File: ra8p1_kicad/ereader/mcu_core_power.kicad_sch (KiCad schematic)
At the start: 17 parts, among them U1 R7KA8P1KFLCAC#UC0

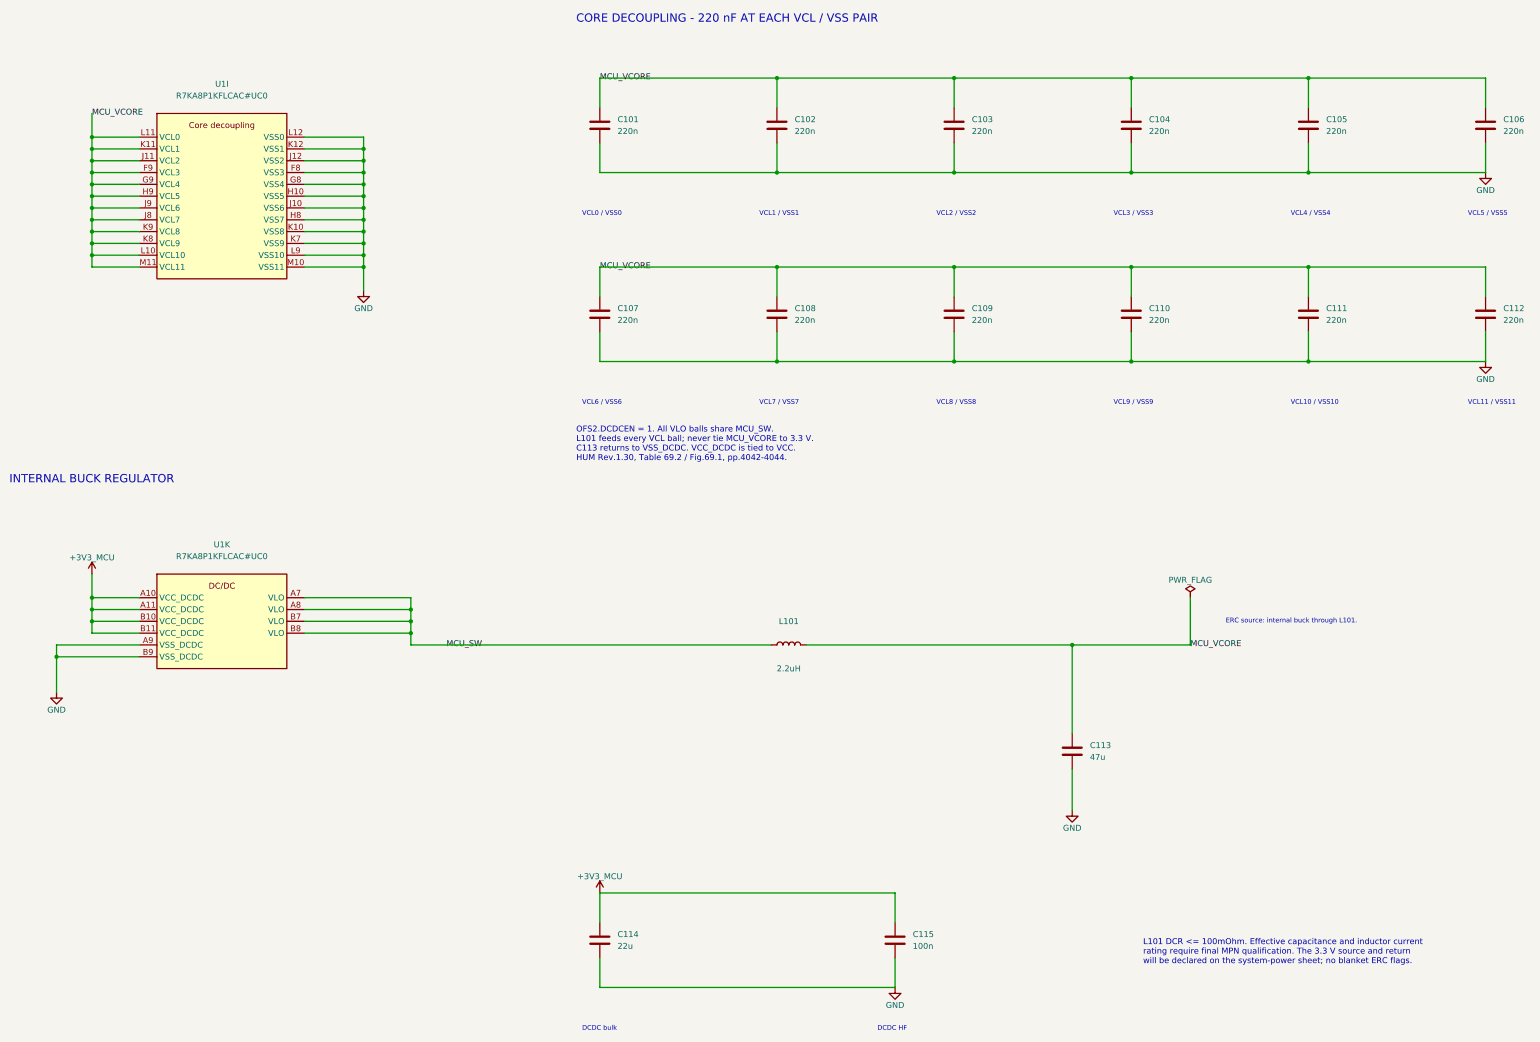
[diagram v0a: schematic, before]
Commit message: feat(hardware): add RA8P1 boot debug draft and refine schematic presentation
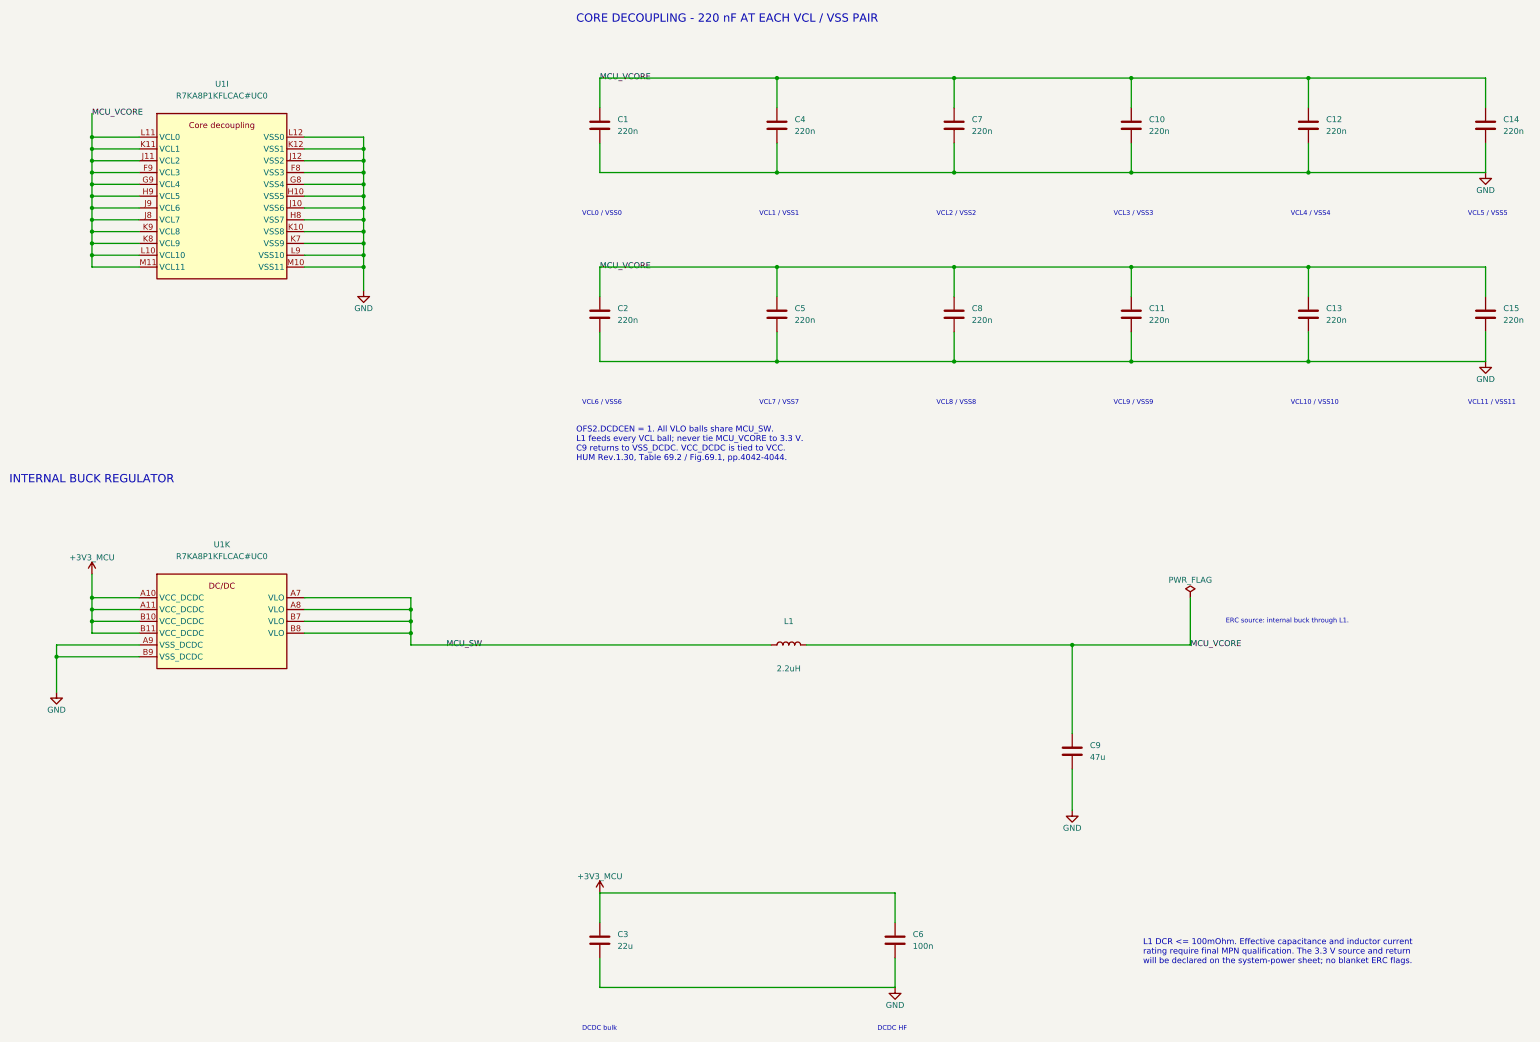
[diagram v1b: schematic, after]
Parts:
- L1: renamed from L101; Manufacturer_Name (none) -> TDK; Manufacturer_Part_Number (none) -> SPM5020T-2R2M-LR; Selection_Basis (none) -> Renesas R01AN7883EU0110 Table 3; 2.2uH +/-20%, DCR max 40.7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
- renumbered C101 to C1, C104 to C10, C110 to C11, C105 to C12, C111 to C13, C106 to C14, C112 to C15, C107 to C2, C114 to C3, C102 to C4, C108 to C5, C115 to C6, C103 to C7, C109 to C8, C113 to C9
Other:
- note added: "ERC source: internal buck through L1."
- note added: "L1 DCR <= 100mOhm. Effective capacitance and inductor current rating require final MPN qualification. The 3.3 V source and return will be declared on the system-power sheet; no blanket ERC flags."
- note added: "OFS2.DCDCEN = 1. All VLO balls share MCU_SW. L1 feeds every VCL ball; never tie MCU_VCORE to 3.3 V. C9 returns to VSS_DCDC. VCC_DCDC is tied to VCC. HUM Rev.1.30, Table 69.2 / Fig.69.1, pp.4042-4044."
- note removed: "ERC source: internal buck through L101."
- note removed: "L101 DCR <= 100mOhm. Effective capacitance and inductor current rating require final MPN qualification. The 3.3 V source and return will be declared on the system-power sheet; no blanket ERC flags."
- note removed: "OFS2.DCDCEN = 1. All VLO balls share MCU_SW. L101 feeds every VCL ball; never tie MCU_VCORE to 3.3 V. C113 returns to VSS_DCDC. VCC_DCDC is tied to VCC. HUM Rev.1.30, Table 69.2 / Fig.69.1, pp.4042-4044."

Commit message: feat(hardware): track schematic BOM and DigiKey sourcing risks
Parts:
- C1, C10, C11, C12, C13, C14, C15, C2, C4, C5, C6, C7, C8: Procurement_Status (none) -> TBD - exact MPN, ratings and DigiKey sourcing required
- C3, C9: Procurement_Status (none) -> TBD - verify effective capacitance under DC bias; source ex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
- L1: DigiKey_Part_Number (none) -> 445-174497-1-ND; DigiKey_URL (none) -> https://www.digikey.com/en/products/detail/tdk/SPM5020T-2R2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; Procurement_Status (none) -> Candidate - reference recommended; validation pending; Sourcing_Snapshot (none) -> 2026-09-05 indexed: stock 1149; USD CT 1:1.35 / 10:1.111 / 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
- U1: DigiKey_Part_Number (none) -> 559-R7KA8P1KFLCAC#UC0-ND; DigiKey_URL (none) -> https://www.digikey.com/en/products/detail/renesas-electron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; Procurement_Status (none) -> HOLD - DigiKey discontinued; qualify orderable RA8P1 suffix; Sourcing_Snapshot (none) -> 2026-09-05 indexed: stock 1; USD 29.47; no backorders. Dist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

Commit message: feat(hardware): add Mouser sourcing and qualify MCU pull-up resistors
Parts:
- U1: Mouser Part Number (none) -> 968-R7KA8P1KFLCACUC0; Mouser Price/Stock (none) -> 2026-09-05 browser: 317 in stock; USD 1:29.47 / 10:23.82 / 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; Mouser_URL (none) -> https://www.mouser.com/en/ProductDetail/Renesas-Electronics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; Procurement_Status HOLD - DigiKey discontinued; qualify orderable RA8P1 suffix -> Retain exact UC0 - Mouser stock verified; circuit qualifica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
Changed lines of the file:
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@@
 			)
 		)
+		(property "Mouser_URL" ""
+			(at 193.04 154.94 90)
+			(hide yes)
+			(show_name no)
+			(do_not_autoplace no)
+			(effects
+				(font
+					(size 1.27 1.27)
+				)
+			)
+		)
 		(pin "1"
 		)
@@
 			)
 		)
-		(property "Mouser Part Number" ""
+		(property "Mouser Part Number" "968-R7KA8P1KFLCACUC0"
 			(at 71.12 144.78 0)
 			(hide yes)
@@
 			)
 		)
-		(property "Mouser Price/Stock" ""
+		(property "Mouser Price/Stock" "2026-09-05 browser: 317 in stock; USD 1:29.47 / 10:23.82 / 25:22.75 / 100:21.71 / 189:21.70; MOQ 1, multiple 1. Recheck before order."
 			(at 71.12 144.78 0)
 			(hide yes)
@@
 			)
 		)
-		(property "Procurement_Status" "HOLD - DigiKey discontinued; qualify orderable RA8P1 suffix"
+		(property "Procurement_Status" "Retain exact UC0 - Mouser stock verified; circuit qualification ongoing"
 			(at 71.12 144.78 0)
 			(hide yes)
@@
 			)
 		)
+		(property "Mouser_URL" "https://www.mouser.com/en/ProductDetail/Renesas-Electronics/R7KA8P1KFLCACUC0?qs=2FehpBK1j97Anbj%252BfZIC1A%3D%3D"
+			(at 71.12 144.78 0)
+			(hide yes)
+			(show_name no)
+			(do_not_autoplace no)
+			(effects
+				(font
+					(size 1.27 1.27)
+				)
+			)
+		)
 		(pin "A10"
 		)
@@
 			)
 		)
+		(property "Mouser_URL" ""
+			(at 342.9 43.18 0)
+			(hide yes)
+			(show_name no)
+			(do_not_autoplace no)
+			(effects
+				(font
+					(size 1.27 1.27)
+				)
+			)
+		)
 		(pin "1"
 		)
@@
 			)
 		)
+		(property "Mouser_URL" ""
+			(at 190.5 43.18 0)
+			(hide yes)
+			(show_name no)
+			(do_not_autoplace no)
+			(effects
+				(font
+					(size 1.27 1.27)
+				)
+			)
+		)
 		(pin "1"
 		)
@@
 			)
 		)
+		(property "Mouser_URL" ""
+			(at 228.6 83.82 0)
+			(hide yes)
+			(show_name no)
+			(do_not_autoplace no)
+			(effects
+				(font
+					(size 1.27 1.27)
+				)
+			)
+		)
 		(pin "1"
 		)
@@
 			)
 		)
+		(property "Mouser_URL" ""
+			(at 254 177.8 0)
+			(hide yes)
+			(show_name no)
+			(do_not_autoplace no)
+			(effects
+				(font
+					(size 1.27 1.27)
+				)
+			)
+		)
 		(pin "1"
 		)
@@
 			)
 		)
+		(property "Mouser_URL" ""
+			(at 266.7 83.82 0)
+			(hide yes)
+			(show_name no)
+			(do_not_autoplace no)
+			(effects
+				(font
+					(size 1.27 1.27)
+				)
+			)
+		)
 		(pin "1"
 		)
@@
 			)
 		)
+		(property "Mouser_URL" ""
+			(at 342.9 83.82 0)
+			(hide yes)
+			(show_name no)
+			(do_not_autoplace no)
+			(effects
+				(font
+					(size 1.27 1.27)
+				)
+			)
+		)
 		(pin "1"
 		)
@@
 			)
 		)
+		(property "Mouser_URL" ""
+			(at 304.8 83.82 0)
+			(hide yes)
+			(show_name no)
+			(do_not_autoplace no)
+			(effects
+				(font
+					(size 1.27 1.27)
+				)
+			)
+		)
 		(pin "1"
 		)
@@
 			)
 		)
+		(property "Mouser_URL" ""
+			(at 228.6 43.18 0)
+			(hide yes)
+			(show_name no)
+			(do_not_autoplace no)
+			(effects
+				(font
+					(size 1.27 1.27)
+				)
+			)
+		)
 		(pin "1"
 		)
@@
 			)
 		)
+		(property "Mouser_URL" ""
+			(at 304.8 43.18 0)
+			(hide yes)
+			(show_name no)
+			(do_not_autoplace no)
+			(effects
+				(font
+					(size 1.27 1.27)
+				)
+			)
+		)
 		(pin "1"
 		)
@@
 			)
 		)
+		(property "Mouser_URL" ""
+			(at 152.4 83.82 0)
+			(hide yes)
+			(show_name no)
+			(do_not_autoplace no)
+			(effects
+				(font
+					(size 1.27 1.27)
+				)
+			)
+		)
 		(pin "1"
 		)
@@
 			)
 		)
+		(property "Mouser_URL" ""
+			(at 190.5 83.82 0)
+			(hide yes)
+			(show_name no)
+			(do_not_autoplace no)
+			(effects
+				(font
+					(size 1.27 1.27)
+				)
+			)
+		)
 		(pin "1"
 		)
@@
 			)
 		)
+		(property "Mouser_URL" ""
+			(at 152.4 218.44 0)
+			(hide yes)
+			(show_name no)
+			(do_not_autoplace no)
+			(effects
+				(font
+					(size 1.27 1.27)
+				)
+			)
+		)
 		(pin "1"
 		)
@@
 			)
 		)
+		(property "Mouser_URL" ""
+			(at 215.9 218.44 0)
+			(hide yes)
+			(show_name no)
+			(do_not_autoplace no)
+			(effects
+				(font
+					(size 1.27 1.27)
+				)
+			)
+		)
 		(pin "1"
 		)
@@
 			)
 		)
-		(property "Mouser Part Number" ""
+		(property "Mouser Part Number" "968-R7KA8P1KFLCACUC0"
 			(at 71.12 45.72 0)
 			(hide yes)
@@
 			)
 		)
-		(property "Mouser Price/Stock" ""
+		(property "Mouser Price/Stock" "2026-09-05 browser: 317 in stock; USD 1:29.47 / 10:23.82 / 25:22.75 / 100:21.71 / 189:21.70; MOQ 1, multiple 1. Recheck before order."
 			(at 71.12 45.72 0)
 			(hide yes)
@@
 			)
 		)
-		(property "Procurement_Status" "HOLD - DigiKey discontinued; qualify orderable RA8P1 suffix"
+		(property "Procurement_Status" "Retain exact UC0 - Mouser stock verified; circuit qualification ongoing"
 			(at 71.12 45.72 0)
 			(hide yes)
@@
 			)
 		)
+		(property "Mouser_URL" "https://www.mouser.com/en/ProductDetail/Renesas-Electronics/R7KA8P1KFLCACUC0?qs=2FehpBK1j97Anbj%252BfZIC1A%3D%3D"
+			(at 71.12 45.72 0)
+			(hide yes)
+			(show_name no)
+			(do_not_autoplace no)
+			(effects
+				(font
+					(size 1.27 1.27)
+				)
+			)
+		)
 		(pin "L11"
 		)
@@
 			)
 		)
+		(property "Mouser_URL" ""
+			(at 152.4 43.18 0)
+			(hide yes)
+			(show_name no)
+			(do_not_autoplace no)
+			(effects
+				(font
+					(size 1.27 1.27)
+				)
+			)
+		)
 		(pin "1"
 		)
@@
 			(at 266.7 43.18 0)
 			(hide yes)
+			(show_name no)
+			(do_not_autoplace no)
+			(effects
+				(font
+					(size 1.27 1.27)
+				)
+			)
+		)
+		(property "Mouser_URL" ""
+			(at 266.7 43.18 0)
+			(hide yes)

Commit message: docs(hardware): qualify bulk-capacitor sourcing status
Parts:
- C3: DigiKey_Part_Number (none) -> 490-6515-1-ND; DigiKey_URL (none) -> https://www.digikey.com/en/products/detail/murata-electroni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; Manufacturer_Name (none) -> Murata Electronics; Manufacturer_Part_Number (none) -> GRM31CR70J226KE19L; Procurement_Status TBD - verify effective capacitance under DC bias; source ex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 -> Candidate - validate DC bias, temperature and lifecycle bef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; Selection_Basis (none) -> Renesas Quick Design Guide Table3 recommended family; 22uF 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; Sourcing_Snapshot (none) -> 2026-09-05 DigiKey indexed stock110912; Active;17wk;USD1:1.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
- C9: Procurement_Status TBD - verify effective capacitance under DC bias; source ex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 -> HOLD - exact 47uF MPN not approved; resolve reference-part 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; Selection_Basis (none) -> Do not approve GRM32ER70J476KE20L solely from Renesas examp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; Sourcing_Snapshot (none) -> 2026-09-05 live Mouser search: GRM32ER70J476KE20L stock7034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
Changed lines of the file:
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@@
 			)
 		)
-		(property "Procurement_Status" "TBD - verify effective capacitance under DC bias; source exact MPN"
+		(property "Procurement_Status" "HOLD - exact 47uF MPN not approved; resolve reference-part lifecycle and effective capacitance"
 			(at 254 177.8 0)
 			(hide yes)
@@
 			)
 		)
-		(property "Sourcing_Snapshot" ""
+		(property "Sourcing_Snapshot" "2026-09-05 live Mouser search: GRM32ER70J476KE20L stock7034, End of Life; DigiKey indexed stock0 Active (conflict)"
 			(at 254 177.8 0)
 			(hide yes)
@@
 		)
 		(property "Mouser_URL" ""
+			(at 254 177.8 0)
+			(hide yes)
+			(show_name no)
+			(do_not_autoplace no)
+			(effects
+				(font
+					(size 1.27 1.27)
+				)
+			)
+		)
+		(property "Selection_Basis" "Do not approve GRM32ER70J476KE20L solely from Renesas example: Mouser EOL flag; replacement and bias qualification required"
 			(at 254 177.8 0)
 			(hide yes)
@@
 			)
 		)
-		(property "Datasheet" ""
+		(property "Datasheet" "https://search.murata.co.jp/Ceramy/image/img/A01X/G101/ENG/GRM31CR70J226KE19-01CA.pdf"
 			(at 152.4 218.44 0)
+			(hide yes)
 			(show_name no)
 			(do_not_autoplace no)
@@
 			)
 		)
-		(property "DigiKey_Part_Number" ""
+		(property "DigiKey_Part_Number" "490-6515-1-ND"
 			(at 152.4 218.44 0)
 			(hide yes)
@@
 			)
 		)
-		(property "DigiKey_URL" ""
+		(property "DigiKey_URL" "https://www.digikey.com/en/products/detail/murata-electronics/GRM31CR70J226KE19L/3845712"
 			(at 152.4 218.44 0)
 			(hide yes)
@@
 			)
 		)
-		(property "Procurement_Status" "TBD - verify effective capacitance under DC bias; source exact MPN"
+		(property "Procurement_Status" "Candidate - validate DC bias, temperature and lifecycle before release"
 			(at 152.4 218.44 0)
 			(hide yes)
@@
 			)
 		)
-		(property "Sourcing_Snapshot" ""
+		(property "Sourcing_Snapshot" "2026-09-05 DigiKey indexed stock110912; Active;17wk;USD1:1.00,10:0.636,100:0.4468"
 			(at 152.4 218.44 0)
 			(hide yes)
@@
 			(at 152.4 218.44 0)
 			(hide yes)
+			(show_name no)
+			(do_not_autoplace no)
+			(effects
+				(font
+					(size 1.27 1.27)
+				)
+			)
+		)
+		(property "Manufacturer_Name" "Murata Electronics"
+			(at 152.4 218.44 0)
+			(hide yes)
+			(show_name no)
+			(do_not_autoplace no)
+			(effects
+				(font
+					(size 1.27 1.27)
+				)
+			)
+		)
+		(property "Manufacturer_Part_Number" "GRM31CR70J226KE19L"
+			(at 152.4 218.44 0)
+			(hide yes)
+			(show_name no)
+			(do_not_autoplace no)
+			(effects
+				(font
+					(size 1.27 1.27)
+				)
+			)
+		)
+		(property "Selection_Basis" "Renesas Quick Design Guide Table3 recommended family; 22uF +/-10% 6.3V X7R; effective capacitance and lifecycle approval pending"
+			(at 152.4 218.44 0)
+			(hide yes)

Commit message: feat(hardware): source and screen MCU bypass capacitors
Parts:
- C6: DigiKey_Part_Number (none) -> 445-1314-1-ND; DigiKey_URL (none) -> https://www.digikey.com/en/products/detail/tdk-corporation/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; Manufacturer_Name (none) -> TDK; Manufacturer_Part_Number (none) -> C1608X7R1H104K080AA; Procurement_Status TBD - exact MPN, ratings and DigiKey sourcing required -> Selected - nominal DC-bias screened; final rail and PDN qua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; Selection_Basis (none) -> 100 nF +/-10%, 50 V X7R. +3V3_MCU bypass. TDK nominal DC-bi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; Sourcing_Snapshot (none) -> 2026-09-05: TDK Production; DigiKey Active, 374087 in stock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
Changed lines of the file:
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@@
 		(property "Datasheet" ""
 			(at 342.9 43.18 0)
+			(hide yes)
 			(show_name no)
 			(do_not_autoplace no)
@@
 		(property "Datasheet" ""
 			(at 190.5 43.18 0)
+			(hide yes)
 			(show_name no)
 			(do_not_autoplace no)
@@
 		(property "Datasheet" ""
 			(at 228.6 83.82 0)
+			(hide yes)
 			(show_name no)
 			(do_not_autoplace no)
@@
 		(property "Datasheet" ""
 			(at 254 177.8 0)
+			(hide yes)
 			(show_name no)
 			(do_not_autoplace no)
@@
 		(property "Datasheet" ""
 			(at 266.7 83.82 0)
+			(hide yes)
 			(show_name no)
 			(do_not_autoplace no)
@@
 		(property "Datasheet" ""
 			(at 342.9 83.82 0)
+			(hide yes)
 			(show_name no)
 			(do_not_autoplace no)
@@
 		(property "Datasheet" ""
 			(at 304.8 83.82 0)
+			(hide yes)
 			(show_name no)
 			(do_not_autoplace no)
@@
 		(property "Datasheet" ""
 			(at 228.6 43.18 0)
+			(hide yes)
 			(show_name no)
 			(do_not_autoplace no)
@@
 		(property "Datasheet" ""
 			(at 304.8 43.18 0)
+			(hide yes)
 			(show_name no)
 			(do_not_autoplace no)
@@
 		(property "Datasheet" ""
 			(at 152.4 83.82 0)
+			(hide yes)
 			(show_name no)
 			(do_not_autoplace no)
@@
 		(property "Datasheet" ""
 			(at 190.5 83.82 0)
+			(hide yes)
 			(show_name no)
 			(do_not_autoplace no)
@@
 			)
 		)
-		(property "Datasheet" ""
+		(property "Datasheet" "https://product.tdk.com/en/search/capacitor/ceramic/mlcc/info?part_no=C1608X7R1H104K080AA"
 			(at 215.9 218.44 0)
+			(hide yes)
 			(show_name no)
 			(do_not_autoplace no)
@@
 			)
 		)
-		(property "DigiKey_Part_Number" ""
+		(property "DigiKey_Part_Number" "445-1314-1-ND"
 			(at 215.9 218.44 0)
 			(hide yes)
@@
 			)
 		)
-		(property "DigiKey_URL" ""
+		(property "DigiKey_URL" "https://www.digikey.com/en/products/detail/tdk-corporation/C1608X7R1H104K080AA/513811"
 			(at 215.9 218.44 0)
 			(hide yes)
@@
 			)
 		)
-		(property "Procurement_Status" "TBD - exact MPN, ratings and DigiKey sourcing required"
+		(property "Procurement_Status" "Selected - nominal DC-bias screened; final rail and PDN qualification open"
 			(at 215.9 218.44 0)
 			(hide yes)
@@
 			)
 		)
-		(property "Sourcing_Snapshot" ""
+		(property "Sourcing_Snapshot" "2026-09-05: TDK Production; DigiKey Active, 374087 in stock, 24 weeks; USD 1:0.11, 10:0.06, 100:0.0359."
 			(at 215.9 218.44 0)
 			(hide yes)
@@
 			)
 		)
+		(property "Manufacturer_Name" "TDK"
+			(at 215.9 218.44 0)
+			(hide yes)
+			(show_name no)
+			(do_not_autoplace no)
+			(effects
+				(font
+					(size 1.27 1.27)
+				)
+			)
+		)
+		(property "Manufacturer_Part_Number" "C1608X7R1H104K080AA"
+			(at 215.9 218.44 0)
+			(hide yes)
+			(show_name no)
+			(do_not_autoplace no)
+			(effects
+				(font
+					(size 1.27 1.27)
+				)
+			)
+		)
+		(property "Selection_Basis" "100 nF +/-10%, 50 V X7R. +3V3_MCU bypass. TDK nominal DC-bias curve: interpolated 99.45 nF at 3.3 V; reference data, not guaranteed minimum. See PWR-001 design/power_decoupling.md."
+			(at 215.9 218.44 0)
+			(hide yes)
+			(show_name no)
+			(do_not_autoplace no)
+			(effects
+				(font
+					(size 1.27 1.27)
+				)
+			)
+		)
 		(pin "1"
 		)
@@
 		(property "Datasheet" ""
 			(at 152.4 43.18 0)
+			(hide yes)
 			(show_name no)
 			(do_not_autoplace no)
@@
 		(property "Datasheet" ""
 			(at 266.7 43.18 0)
+			(hide yes)
 			(show_name no)
 			(do_not_autoplace no)
